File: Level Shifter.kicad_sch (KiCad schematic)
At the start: 3 parts, among them Q1 BSS138

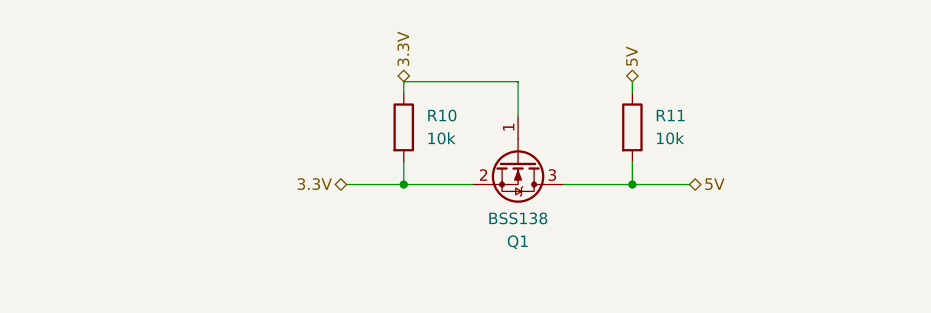
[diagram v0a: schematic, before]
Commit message: bulk caps for power (todo, split 470uF cap so that it can be shorter)
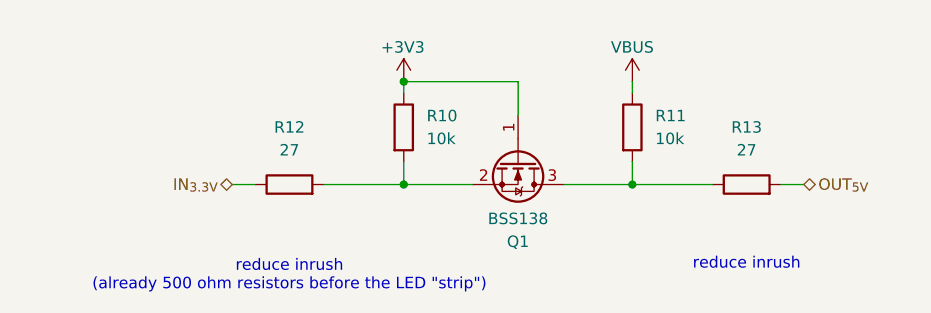
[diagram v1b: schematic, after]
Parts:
- added R12, R13: 27, Resistor_SMD:R_0402_1005Metric, symbol Device:R
- R10, R11: footprint (none) -> Resistor_SMD:R_0402_1005Metric; LCSC (none) -> C25744; MPN (none) -> 0402WGF1002TCE; Manufacturer (none) -> UNIROYAL
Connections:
- net 3.3V: no longer names the net of Q1.2 (S), R10.2
- net 3.3V: now also R12.2; no longer Q1.1 (G), R10.1
- net 5V: no longer names the net of Q1.3 (D), R11.2
- net 5V: now also R13.1; no longer R11.1
- new net +3V3: Q1.1 (G), R10.1
- new net IN_{3.3V}: R12.1
- new net OUT_{5V}: R13.2
- new net VBUS: R11.1
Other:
- note added: "reduce inrush"
- note added: "reduce inrush (already 500 ohm resistors before the LED "strip")"

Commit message: add debug led, make bulk caps smaller, export plate and bottom for rudimentary case
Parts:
- Q1: LCSC (none) -> C52895; MPN (none) -> BSS138; Manufacturer (none) -> ONSEMI
- R12, R13: LCSC C25765 -> C25100; MPN 0402WGF2002TCE -> 0402WGF270JTCE
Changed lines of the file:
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@@
+			)
+		)
+		(property "LCSC" "C52895"
+			(at 133.35 92.71 0)
+			(effects
+				(font
+					(size 1.27 1.27)
+				)
+				(hide yes)
+			)
+		)
+		(property "MPN" "BSS138"
+			(at 133.35 92.71 0)
+			(effects
+				(font
+					(size 1.27 1.27)
+				)
+				(hide yes)
+			)
+		)
+		(property "Manufacturer" "ONSEMI"
+			(at 133.35 92.71 0)
+			(effects
+				(font
+					(size 1.27 1.27)
+				)
+				(hide yes)
 			)
 		)
@@
 			)
 		)
-		(property "LCSC" "C25765"
-			(at 107.95 95.25 0)
-			(effects
-				(font
-					(size 1.27 1.27)
-				)
-				(hide yes)
-			)
-		)
-		(property "MPN" "0402WGF2002TCE"
+		(property "LCSC" "C25100"
+			(at 107.95 95.25 0)
+			(effects
+				(font
+					(size 1.27 1.27)
+				)
+				(hide yes)
+			)
+		)
+		(property "MPN" "0402WGF270JTCE"
 			(at 107.95 95.25 0)
 			(effects
@@
 			)
 		)
-		(property "LCSC" "C25765"
-			(at 158.75 95.25 0)
-			(effects
-				(font
-					(size 1.27 1.27)
-				)
-				(hide yes)
-			)
-		)
-		(property "MPN" "0402WGF2002TCE"
-			(at 158.75 95.25 0)
-			(effects
+		(property "LCSC" "C25100"
+			(at 158.75 95.25 0)
+			(effects
+				(font
+					(size 1.27 1.27)
+				)
+				(hide yes)
+			)
+		)
+		(property "MPN" "0402WGF270JTCE"
+			(at 158.75 95.25 0)
+			(effects

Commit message: fab output changes (part choice updates)
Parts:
- Q1, R10, R11, R12, R13: Type (none) -> SMD
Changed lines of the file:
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@@
+			)
+		)
+		(property "Type" "SMD"
+			(at 120.65 88.9 0)
+			(effects
+				(font
+					(size 1.27 1.27)
+				)
+				(hide yes)
 			)
 		)
@@
 		)
 		(property "Manufacturer" "ONSEMI"
+			(at 133.35 92.71 0)
+			(effects
+				(font
+					(size 1.27 1.27)
+				)
+				(hide yes)
+			)
+		)
+		(property "Type" "SMD"
 			(at 133.35 92.71 0)
 			(effects
@@
 			)
 		)
+		(property "Type" "SMD"
+			(at 107.95 95.25 0)
+			(effects
+				(font
+					(size 1.27 1.27)
+				)
+				(hide yes)
+			)
+		)
 		(pin "1"
 		)
@@
 			)
 		)
+		(property "Type" "SMD"
+			(at 158.75 95.25 0)
+			(effects
+				(font
+					(size 1.27 1.27)
+				)
+				(hide yes)
+			)
+		)
 		(pin "1"
 		)
@@
 			(at 146.05 88.9 0)
 			(effects
+				(font
+					(size 1.27 1.27)
+				)
+				(hide yes)
+			)
+		)
+		(property "Type" "SMD"
+			(at 146.05 88.9 0)
+			(effects
